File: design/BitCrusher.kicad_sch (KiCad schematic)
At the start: 0 parts

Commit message: started primary power distribution design
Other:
- company: (none) -> UNH Resilient Architecture Lab
- title: (none) -> BitCrusher: Affordable, Open Source EMFI Platform
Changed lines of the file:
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@@
 	(generator_version "9.0")
 	(paper "A4")
+	(title_block
+		(title "BitCrusher: Affordable, Open Source EMFI Platform")
+		(rev "0.1")
+		(company "UNH Resilient Architecture Lab")
+		(comment 1 "Author: George Crane")
+	)
 	(sheet
 		(at 30.48 68.58)

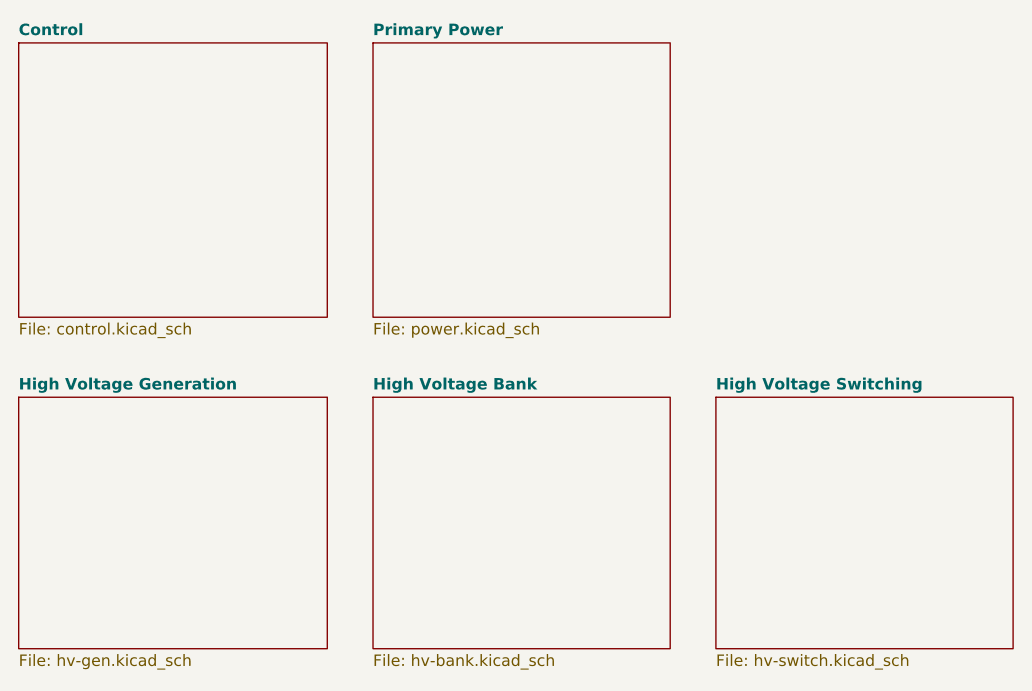
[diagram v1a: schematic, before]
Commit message: added CubeMX files, worked on microcontroller schematic
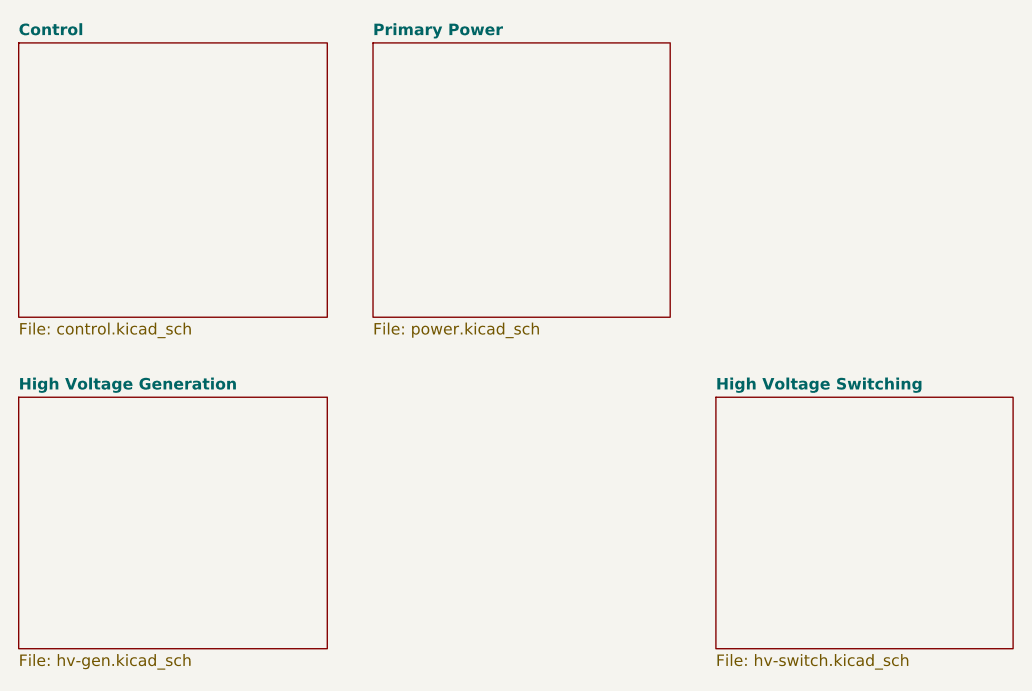
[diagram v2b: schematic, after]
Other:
- removed sheet High Voltage Bank
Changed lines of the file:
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@@
-	)
-	(sheet
-		(at 69.85 68.58)
-		(size 33.02 27.94)
-		(exclude_from_sim no)
-		(in_bom yes)
-		(on_board yes)
-		(dnp no)
-		(fields_autoplaced yes)
-		(stroke
-			(width 0.1524)
-			(type solid)
-		)
-		(fill
-			(color 0 0 0 0.0000)
-		)
-		(property "Sheetname" "High Voltage Bank"
-			(at 69.85 67.8684 0)
-			(effects
-				(font
-					(size 1.27 1.27)
-					(thickness 0.254)
-					(bold yes)
-				)
-				(justify left bottom)
-			)
-		)
-		(property "Sheetfile" "hv-bank.kicad_sch"
-			(at 69.85 97.1046 0)
-			(effects
-				(font
-					(size 1.27 1.27)
-				)
-				(justify left top)
-			)
-		)
-		(instances
-			(project "BitCrusher"
-				(path "/e1be550d-9ce6-42b1-a89a-c00b9d7586dd"
-					(page "5")
-				)
-			)
-		)
 	)
 	(sheet

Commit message: started USB-C interface design
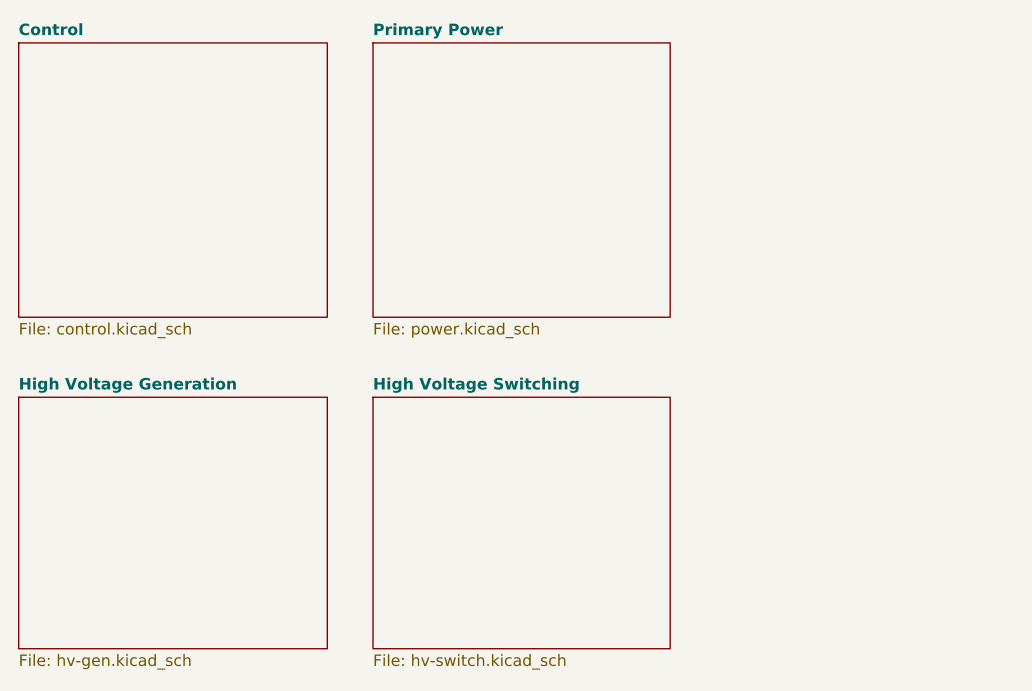
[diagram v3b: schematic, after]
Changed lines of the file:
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@@
 	)
 	(sheet
-		(at 107.95 68.58)
+		(at 69.85 68.58)
 		(size 33.02 27.94)
 		(exclude_from_sim no)
@@
 		)
 		(property "Sheetname" "High Voltage Switching"
-			(at 107.95 67.8684 0)
+			(at 69.85 67.8684 0)
 			(effects
 				(font
@@
 		)
 		(property "Sheetfile" "hv-switch.kicad_sch"
-			(at 107.95 97.1046 0)
+			(at 69.85 97.1046 0)
 			(effects
 				(font
